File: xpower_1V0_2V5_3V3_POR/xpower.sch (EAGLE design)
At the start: 7 parts, among them U1 TLV70233, U2 TLV70225

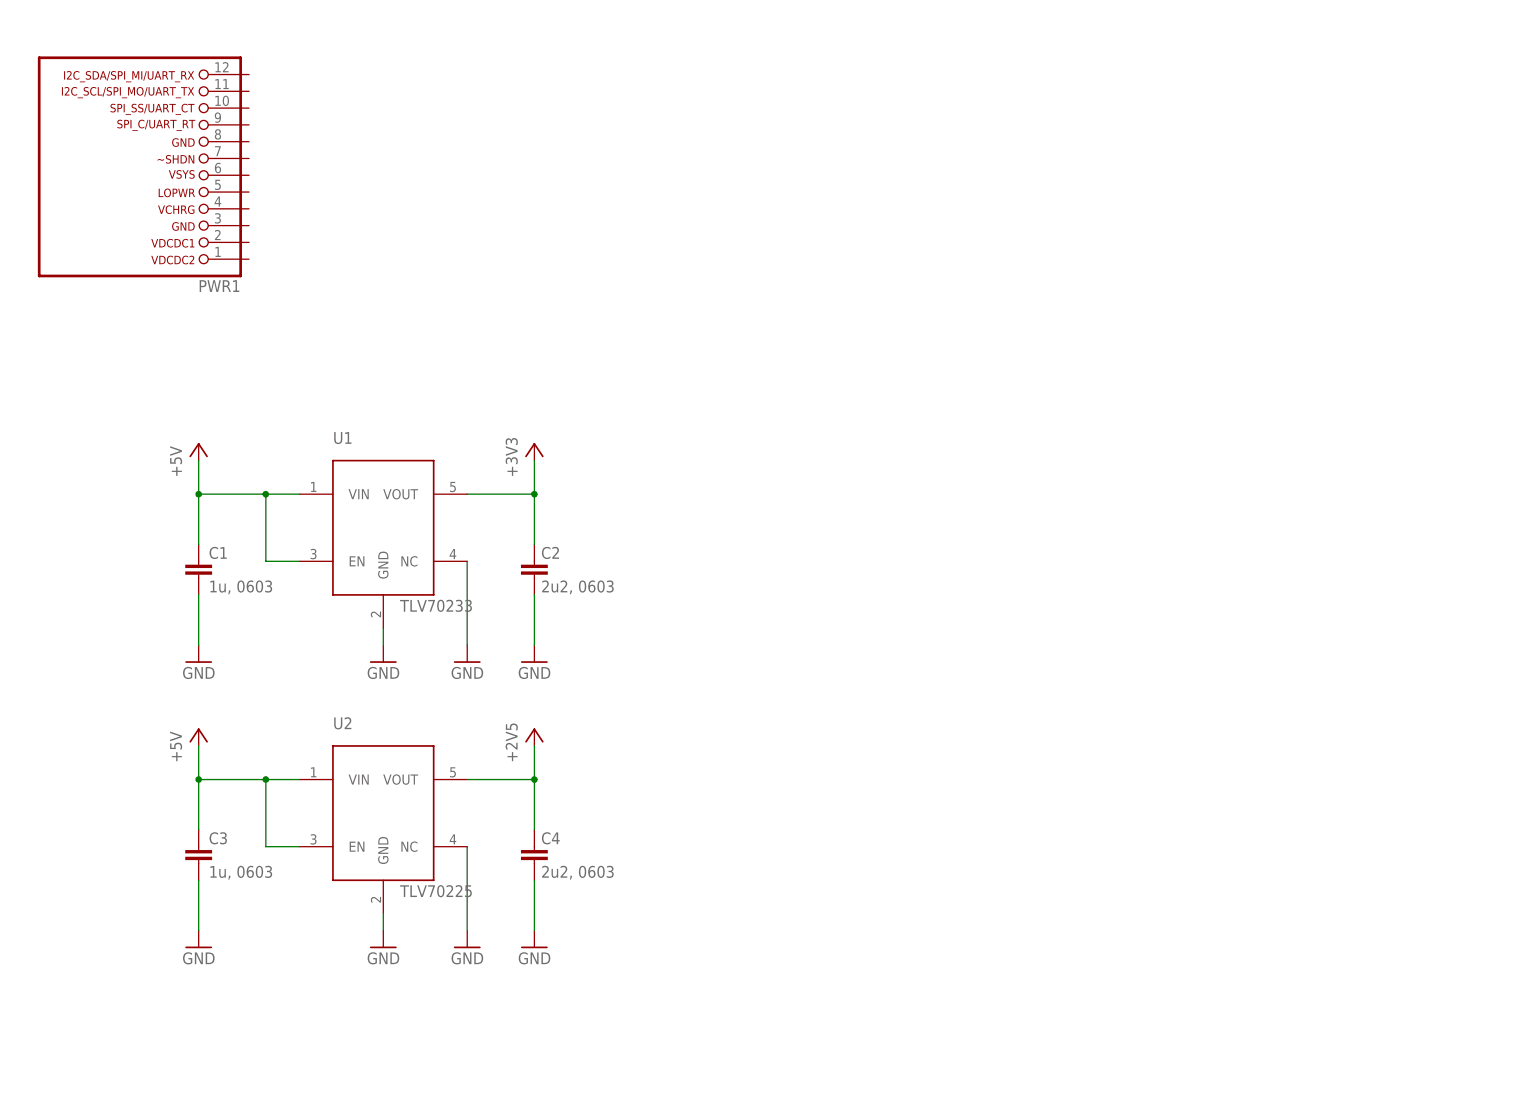
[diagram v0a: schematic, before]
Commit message: WIP: xpower 1V0, 2V5, 3V3 and 5V0 suply with POR output.
Signed-off-by: malo <pavol.malosek@gmail.com>
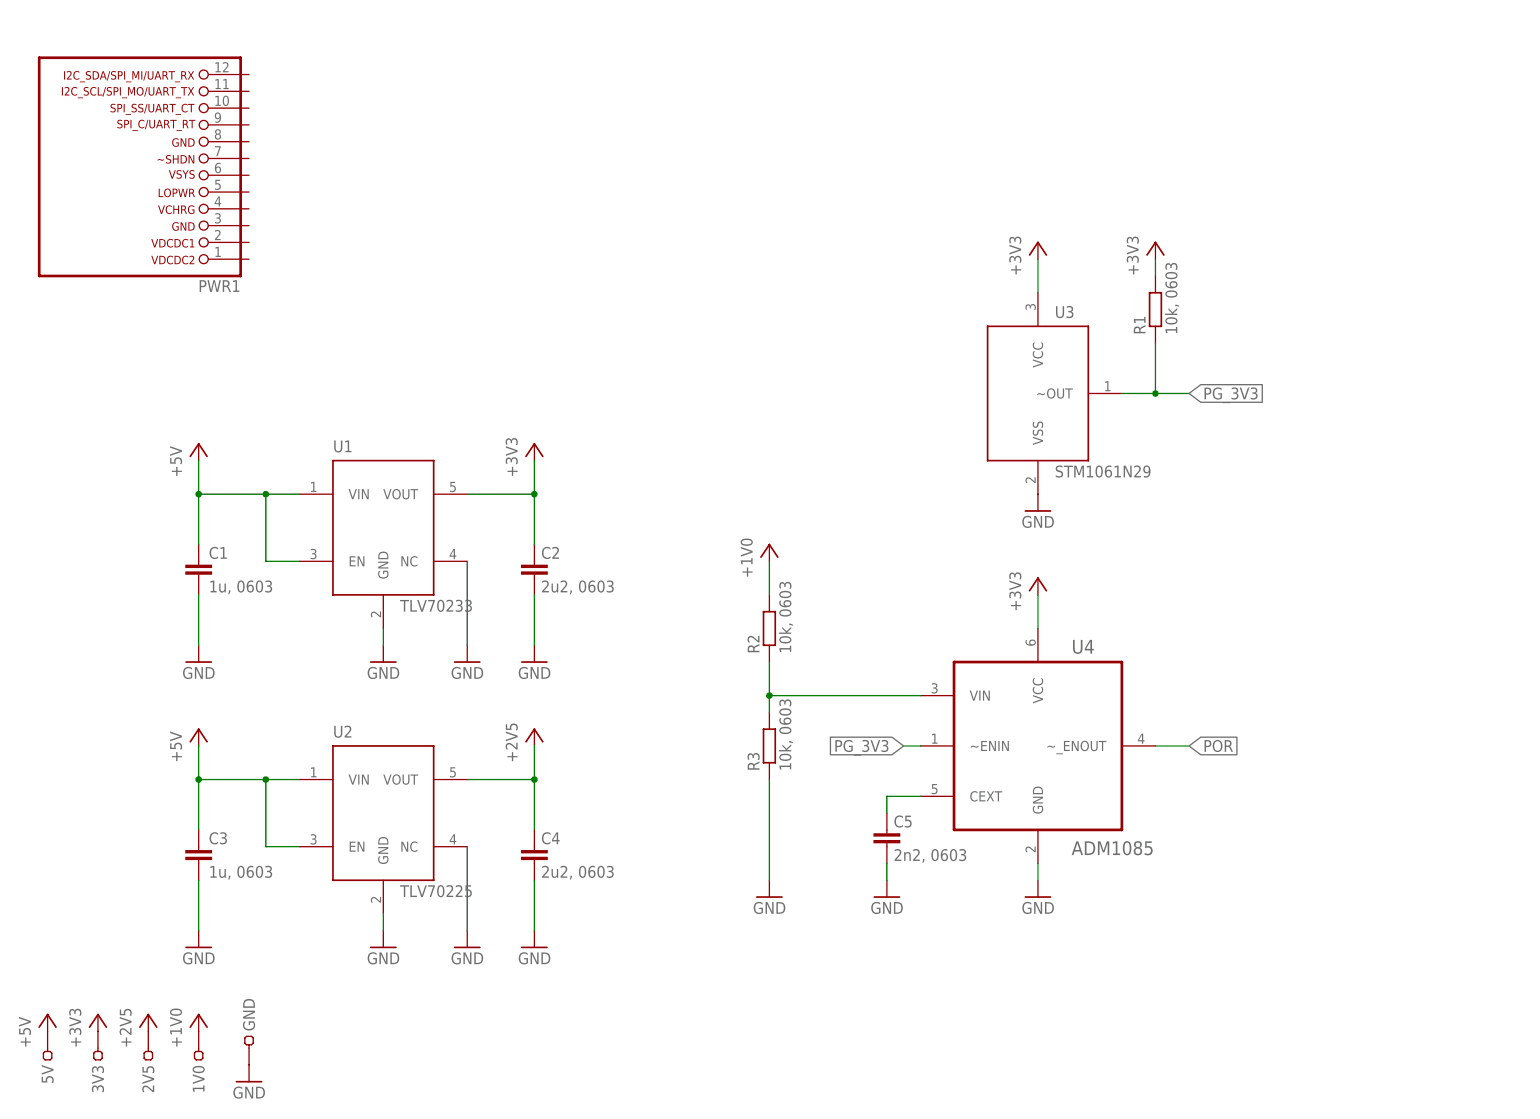
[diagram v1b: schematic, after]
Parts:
- added 1V0, 2V5, 3V3, 5V, GND: TEST-22-MULTICOMP, 25cmsquare:TEST-22-MULTICOMP
- added C5: 2n2, 0603, rcl:C-EUC0603
- added R1, R2, R3: 10k, 0603, rcl:R-EU_R0603
- added U3: STM1061N29, 25cmsquare:STM1061
- added U4: ADM1085, 25cmsquare:ADM1085
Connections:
- new net +1V0: 1V0.1, R2.2
- new net CEXT: C5.1, U4.CEXT
- new net PG_3V3: R1.1, U3.~OUT, U4.~ENIN
- new net POR: U4.~_ENOUT
- new net VIN: R2.1, R3.2, U4.VIN
- net +2V5: now also 2V5.1
- net +3V3: now also 3V3.1, R1.2, U3.VCC, U4.VCC
- net +5V: now also 5V.1
- net GND: now also C5.2, GND.1, R3.1, U3.VSS, U4.GND
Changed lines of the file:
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@@
 <part name="+3V1" library="supply1" deviceset="+3V3" device=""/>
 <part name="+2V1" library="25cmsquare" deviceset="+2V5" device=""/>
+<part name="U3" library="25cmsquare" deviceset="STM1061" device="" value="STM1061N29"/>
+<part name="GND9" library="supply1" deviceset="GND" device=""/>
+<part name="+3V2" library="supply1" deviceset="+3V3" device=""/>
+<part name="R1" library="rcl" deviceset="R-EU_" device="R0603" value="10k, 0603"/>
+<part name="+3V3" library="supply1" deviceset="+3V3" device=""/>
+<part name="U4" library="25cmsquare" deviceset="ADM1085" device=""/>
+<part name="+3V4" library="supply1" deviceset="+3V3" device=""/>
+<part name="GND10" library="supply1" deviceset="GND" device=""/>
+<part name="R2" library="rcl" deviceset="R-EU_" device="R0603" value="10k, 0603"/>
+<part name="R3" library="rcl" deviceset="R-EU_" device="R0603" value="10k, 0603"/>
+<part name="GND11" library="supply1" deviceset="GND" device=""/>
+<part name="C5" library="rcl" deviceset="C-EU" device="C0603" value="2n2, 0603"/>
+<part name="GND12" library="supply1" deviceset="GND" device=""/>
+<part name="U$1" library="25cmsquare" deviceset="+1V0" device=""/>
+<part name="5V" library="25cmsquare" deviceset="TEST-22-MULTICOMP" device=""/>
+<part name="3V3" library="25cmsquare" deviceset="TEST-22-MULTICOMP" device=""/>
+<part name="2V5" library="25cmsquare" deviceset="TEST-22-MULTICOMP" device=""/>
+<part name="GND" library="25cmsquare" deviceset="TEST-22-MULTICOMP" device=""/>
+<part name="P+3" library="supply1" deviceset="+5V" device=""/>
+<part name="+3V5" library="supply1" deviceset="+3V3" device=""/>
+<part name="+2V2" library="25cmsquare" deviceset="+2V5" device=""/>
+<part name="1V0" library="25cmsquare" deviceset="TEST-22-MULTICOMP" device=""/>
+<part name="U$7" library="25cmsquare" deviceset="+1V0" device=""/>
+<part name="GND13" library="supply1" deviceset="GND" device=""/>
 </parts>
 <sheets>
@@
 <instance part="+3V1" gate="G$1" x="96.52" y="109.22"/>
 <instance part="+2V1" gate="G$1" x="96.52" y="63.5"/>
+<instance part="U3" gate="G$1" x="172.72" y="116.84"/>
+<instance part="GND9" gate="1" x="172.72" y="99.06" rot="MR0"/>
+<instance part="+3V2" gate="G$1" x="172.72" y="139.7"/>
+<instance part="R1" gate="G$1" x="190.5" y="129.54" rot="R90"/>
+<instance part="+3V3" gate="G$1" x="190.5" y="139.7"/>
+<instance part="U4" gate="A" x="172.72" y="63.5"/>
+<instance part="+3V4" gate="G$1" x="172.72" y="88.9"/>
+<instance part="GND10" gate="1" x="172.72" y="40.64" rot="MR0"/>
+<instance part="R2" gate="G$1" x="132.08" y="81.28" rot="R90"/>
+<instance part="R3" gate="G$1" x="132.08" y="63.5" rot="R90"/>
+<instance part="GND11" gate="1" x="132.08" y="40.64" rot="MR0"/>
+<instance part="C5" gate="G$1" x="149.86" y="50.8" smashed="yes" rot="MR0">
+<attribute name="NAME" x="150.876" y="51.181" size="1.778" layer="95"/>
+<attribute name="VALUE" x="150.876" y="46.101" size="1.778" layer="96"/>
+</instance>
+<instance part="GND12" gate="1" x="149.86" y="40.64" rot="MR0"/>
+<instance part="U$1" gate="A" x="132.08" y="91.44"/>
+<instance part="5V" gate="G$1" x="22.86" y="20.32" rot="MR270"/>
+<instance part="3V3" gate="G$1" x="30.48" y="20.32" rot="MR270"/>
+<instance part="2V5" gate="G$1" x="38.1" y="20.32" rot="MR270"/>
+<instance part="GND" gate="G$1" x="53.34" y="15.24" rot="MR90"/>
+<instance part="P+3" gate="1" x="22.86" y="22.86"/>
+<instance part="+3V5" gate="G$1" x="30.48" y="22.86"/>
+<instance part="+2V2" gate="G$1" x="38.1" y="20.32"/>
+<instance part="1V0" gate="G$1" x="45.72" y="20.32" rot="MR270"/>
+<instance part="U$7" gate="A" x="45.72" y="20.32"/>
+<instance part="GND13" gate="1" x="53.34" y="12.7" rot="MR0"/>
 </instances>
 <busses>
@@
 <junction x="45.72" y="58.42"/>
 </segment>
+<segment>
+<pinref part="5V" gate="G$1" pin="1"/>
+<pinref part="P+3" gate="1" pin="+5V"/>
+</segment>
 </net>
 <net name="GND" class="0">
@@
 <pinref part="GND7" gate="1" pin="GND"/>
 <wire x1="96.52" y1="43.18" x2="96.52" y2="35.56" width="0.1524" layer="91"/>
+</segment>
+<segment>
+<pinref part="U3" gate="G$1" pin="VSS"/>
+<pinref part="GND9" gate="1" pin="GND"/>
+</segment>
+<segment>
+<pinref part="GND10" gate="1" pin="GND"/>
+<pinref part="U4" gate="A" pin="GND"/>
+<wire x1="172.72" y1="43.18" x2="172.72" y2="45.72" width="0.1524" layer="91"/>
+</segment>
+<segment>
+<pinref part="GND11" gate="1" pin="GND"/>
+<pinref part="R3" gate="G$1" pin="1"/>
+<wire x1="132.08" y1="43.18" x2="132.08" y2="58.42" width="0.1524" layer="91"/>
+</segment>
+<segment>
+<pinref part="C5" gate="G$1" pin="2"/>
+<wire x1="149.86" y1="45.72" x2="149.86" y2="43.18" width="0.1524" layer="91"/>
+<pinref part="GND12" gate="1" pin="GND"/>
+</segment>
+<segment>
+<pinref part="GND" gate="G$1" pin="1"/>
+<pinref part="GND13" gate="1" pin="GND"/>
 </segment>
 </net>
@@
 <junction x="96.52" y="101.6"/>
 </segment>
+<segment>
+<pinref part="U3" gate="G$1" pin="VCC"/>
+<wire x1="172.72" y1="132.08" x2="172.72" y2="137.16" width="0.1524" layer="91"/>
+<pinref part="+3V2" gate="G$1" pin="+3V3"/>
+</segment>
+<segment>
+<pinref part="R1" gate="G$1" pin="2"/>
+<pinref part="+3V3" gate="G$1" pin="+3V3"/>
+<wire x1="190.5" y1="134.62" x2="190.5" y2="137.16" width="0.1524" layer="91"/>
+</segment>
+<segment>
+<pinref part="U4" gate="A" pin="VCC"/>
+<pinref part="+3V4" gate="G$1" pin="+3V3"/>
+<wire x1="172.72" y1="81.28" x2="172.72" y2="86.36" width="0.1524" layer="91"/>
+</segment>
+<segment>
+<pinref part="3V3" gate="G$1" pin="1"/>
+<pinref part="+3V5" gate="G$1" pin="+3V3"/>
+</segment>
 </net>
 <net name="+2V5" class="0">
@@
 <junction x="96.52" y="58.42"/>
 </segment>
-</net>
+<segment>
+<pinref part="2V5" gate="G$1" pin="1"/>
+<pinref part="+2V2" gate="G$1" pin="+2V5"/>
+</segment>
+</net>
+<net name="PG_3V3" class="0">
+<segment>
+<pinref part="U3" gate="G$1" pin="~OUT"/>
+<pinref part="R1" gate="G$1" pin="1"/>
+<wire x1="185.42" y1="116.84" x2="190.5" y2="116.84" width="0.1524" layer="91"/>
+<wire x1="190.5" y1="116.84" x2="190.5" y2="124.46" width="0.1524" layer="91"/>
+<wire x1="190.5" y1="116.84" x2="195.58" y2="116.84" width="0.1524" layer="91"/>
+<junction x="190.5" y="116.84"/>
+<label x="195.58" y="116.84" size="1.778" layer="95" xref="yes"/>
+</segment>
+<segment>
+<pinref part="U4" gate="A" pin="~ENIN"/>
+<wire x1="154.94" y1="63.5" x2="152.4" y2="63.5" width="0.1524" layer="91"/>
+<label x="152.4" y="63.5" size="1.778" layer="95" rot="R180" xref="yes"/>
+</segment>
+</net>
+<net name="POR" class="0">
+<segment>
+<pinref part="U4" gate="A" pin="~_ENOUT"/>
+<wire x1="190.5" y1="63.5" x2="195.58" y2="63.5" width="0.1524" layer="91"/>
+<label x="195.58" y="63.5" size="1.778" layer="95" xref="yes"/>
+</segment>
+</net>
+<net name="VIN" class="0">
+<segment>
+<pinref part="R3" gate="G$1" pin="2"/>
+<pinref part="R2" gate="G$1" pin="1"/>
+<wire x1="132.08" y1="68.58" x2="132.08" y2="71.12" width="0.1524" layer="91"/>
+<pinref part="U4" gate="A" pin="VIN"/>
+<wire x1="132.08" y1="71.12" x2="132.08" y2="76.2" width="0.1524" layer="91"/>
+<wire x1="154.94" y1="71.12" x2="132.08" y2="71.12" width="0.1524" layer="91"/>
+<junction x="132.08" y="71.12"/>
+</segment>
+</net>
+<net name="CEXT" class="0">
+<segment>
+<pinref part="C5" gate="G$1" pin="1"/>
+<pinref part="U4" gate="A" pin="CEXT"/>
+<wire x1="149.86" y1="53.34" x2="149.86" y2="55.88" width="0.1524" layer="91"/>
+<wire x1="149.86" y1="55.88" x2="154.94" y2="55.88" width="0.1524" layer="91"/>
+</segment>
+</net>
+<net name="+1V0" class="0">
+<segment>
+<pinref part="R2" gate="G$1" pin="2"/>
+<wire x1="132.08" y1="86.36" x2="132.08" y2="91.44" width="0.1524" layer="91"/>
+<pinref part="U$1" gate="A" pin="+1V0"/>
+</segment>
+<segment>
+<pinref part="1V0" gate="G$1" pin="1"/>
+<pinref part="U$7" gate="A" pin="+1V0"/>
+</segment>
+</net>

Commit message: WIP: xpower - added 1V0
Signed-off-by: malo <pavol.malosek@gmail.com>
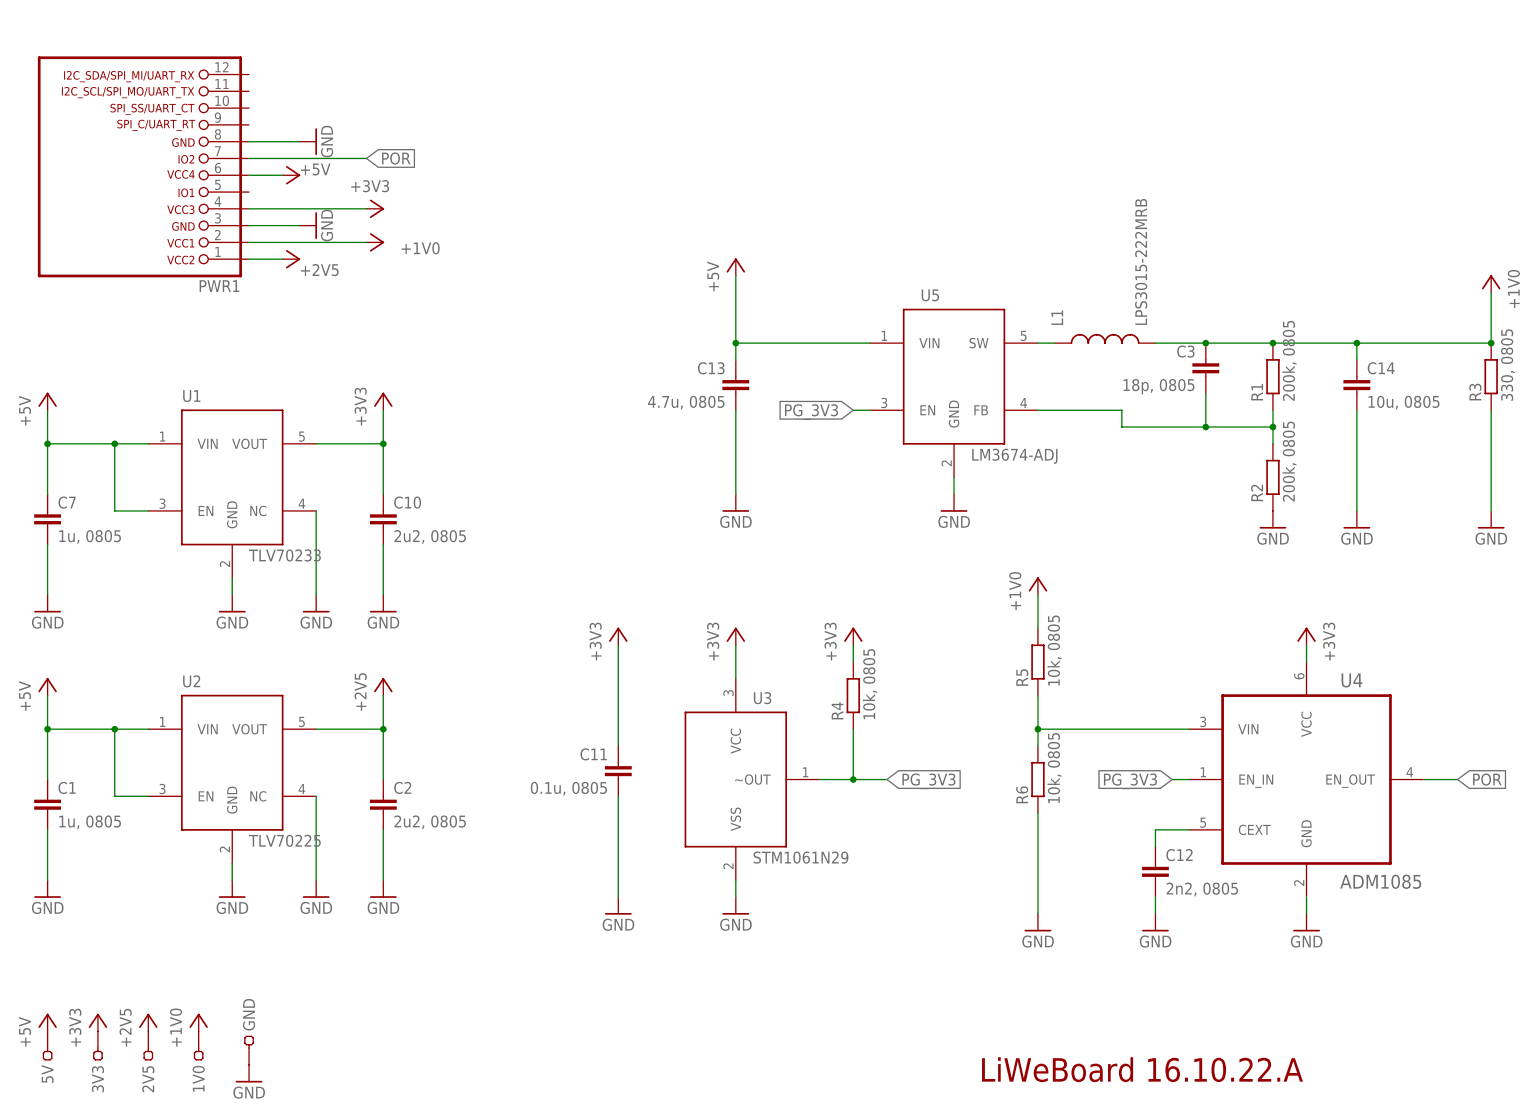
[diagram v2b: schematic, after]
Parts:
- removed C4: 2u2, 0603, rcl:C-EUC0603
- removed C5: 2n2, 0603, rcl:C-EUC0603
- added C10: 2u2, 0805, rcl:C-EUC0805
- added C11: 0.1u, 0805, rcl:C-EUC0805
- added C12: 2n2, 0805, rcl:C-EUC0805
- added C13: 4.7u, 0805, rcl:C-EUC0805
- added C14: 10u, 0805, rcl:C-EUC0805
- added C7: 1u, 0805, rcl:C-EUC0805
- added L1: LPS3015-222MRB, inductor-coilcraft:LPS3015
- added R4, R5, R6: 10k, 0805, rcl:R-EU_R0805
- added U5: LM3674-ADJ, 25cmsquare:LM3674-ADJ
- C1: value 1u, 0603 -> 1u, 0805; device rcl:C-EUC0603 -> rcl:C-EUC0805
- C2: value 2u2, 0603 -> 2u2, 0805; device rcl:C-EUC0603 -> rcl:C-EUC0805
- C3: value 1u, 0603 -> 18p, 0805; device rcl:C-EUC0603 -> rcl:C-EUC0805
- R1, R2: value 10k, 0603 -> 200k, 0805; device rcl:R-EU_R0603 -> rcl:R-EU_R0805
- R3: value 10k, 0603 -> 330, 0805; device rcl:R-EU_R0603 -> rcl:R-EU_R0805
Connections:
- removed net N$2: C1.2
- removed net N$4: C3.2
- new net FB: C3.2, R1.1, R2.2, U5.FB
- new net L: L1.1, U5.SW
- net +1V0: now also C14.1, C3.1, L1.2, PWR1.2, R1.2, R3.2, R5.2; no longer R2.2
- net +2V5: now also C2.1, PWR1.1; no longer C4.1
- net +3V3: now also C10.1, C11.1, PWR1.4, R4.2; no longer C2.1, R1.2
- net +5V: now also C13.1, C7.1, PWR1.6, U5.VIN; no longer C3.1
- net CEXT: now also C12.1; no longer C5.1
- net GND: now also C1.2, C10.2, C11.2, C12.2, C13.2, C14.2, C7.2, PWR1.3, PWR1.8, R2.1, R6.1, U5.GND; no longer C4.2, C5.2
- net PG_3V3: now also R4.1, U4.EN_IN, U5.EN; no longer R1.1, U4.~ENIN
- net POR: now also PWR1.7, U4.EN_OUT; no longer U4.~_ENOUT
- net VIN: now also R5.1, R6.2; no longer R2.1, R3.2
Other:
- note added: "LiWeBoard 16.10.22.A"
- moved on the sheet: C1, C2, C3, R1, R2, R3, U1, U2, U3, U4

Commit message: WIP: xpower - added USB
Signed-off-by: malo <pavol.malosek@gmail.com>
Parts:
- added C15, C6: 100n, 0805, rcl:C-EUC0805
- added C9: 4.7n, 0805, rcl:C-EUC0805
- added L3: BLM21PG331SH1D, resistor:L-USL0805
- added R8: 1M, 0805, rcl:R-EU_R0805
- added TP1: TPTP14R, testpad:TPTP14R
- added U$5: ZX62D-B-5PA8, pma:ZX62D-B-5PA8
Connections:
- new net D_N: PWR1.10, U$5.D-
- new net D_P: PWR1.9, U$5.D+
- new net N$2: C6.1, L3.2, U$5.VBUS
- new net PE: C9.1, R8.2, U$5.MTN1, U$5.MTN2, U$5.MTN3, U$5.MTN4
- net +5V: now also C15.1, L3.1
- net GND: now also C15.2, C6.2, C9.2, R8.1, U$5.GND
- net PG_3V3: now also TP1.TP
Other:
- moved on the sheet: C13
